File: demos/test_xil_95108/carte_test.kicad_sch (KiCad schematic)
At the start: 42 parts, among them J1 DB25, J2 DB9FEM, K1 CONN_3, P2 CONN_3, P3 CONN_2, P4 CONN_2X2, SW1 SW_PUSH, SW2 SW_PUSH, U1 TDA8702, U2 XC95108PC84, U3 LM7805, U4 74HC04, U5 RAM_32KO, U6 LM318N, X1 10MHz

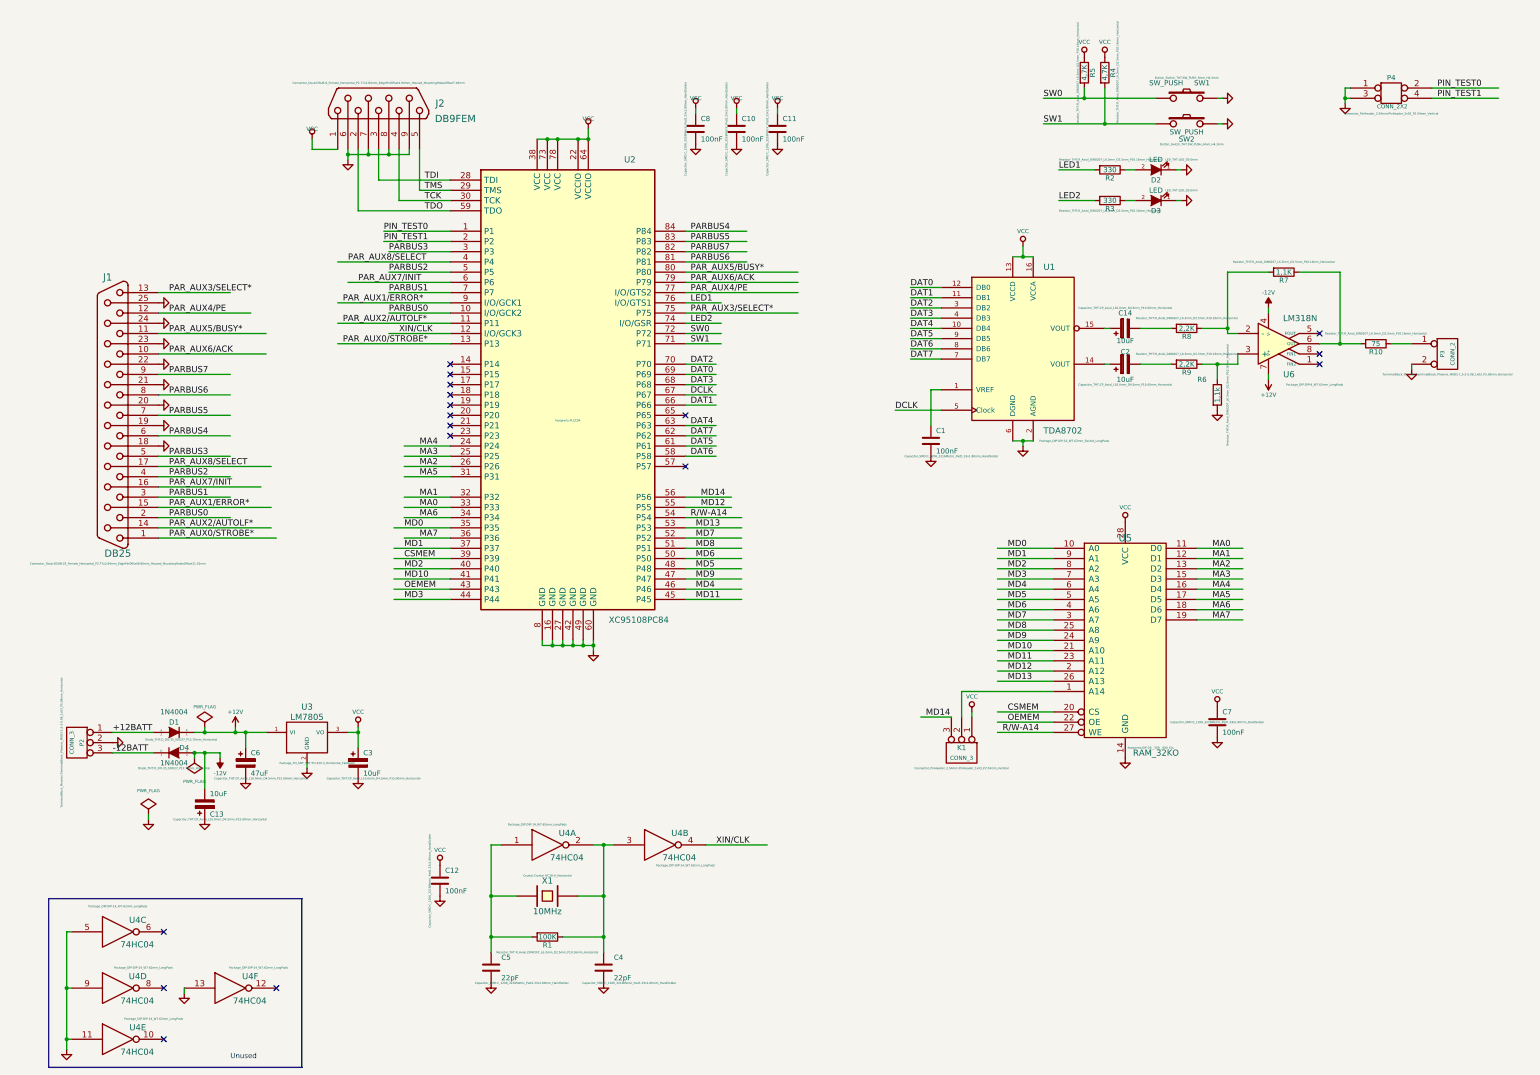
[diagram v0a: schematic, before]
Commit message: feat: update kicad to 9.0.0+dfsg-1
Signed-off-by: lhdjply <lhdjply@126.com>
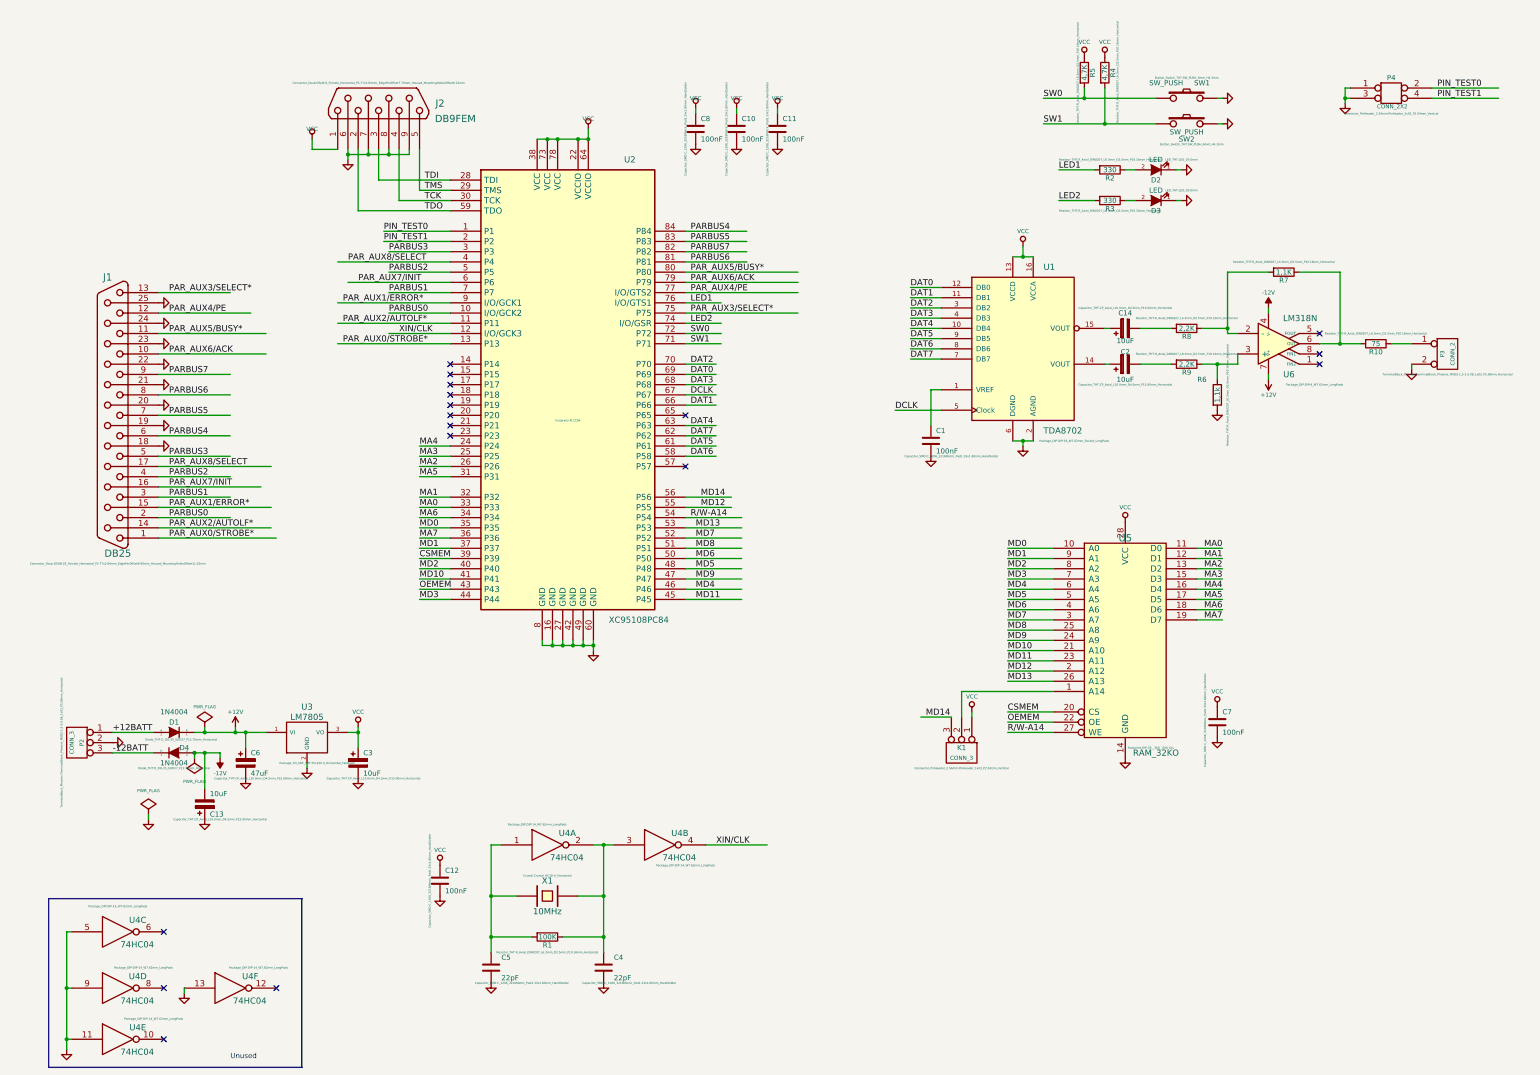
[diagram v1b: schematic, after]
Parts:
- J2: footprint Connector_Dsub:DSUB-9_Female_Horizontal_P2.77x2.84mm_EdgePinOffset4.94mm_Housed_MountingHolesOffset7.48mm -> Connector_Dsub:DSUB-9_Female_Horizontal_P2.77x2.84mm_EdgePinOffset7.70mm_Housed_MountingHolesOffset9.12mm
